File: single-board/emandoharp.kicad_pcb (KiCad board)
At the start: 2 copper layers, 120 x 170 mm, 117 parts, among them P1 piezo, P10 piezo, P11 piezo, P12 piezo, P13 piezo, P14 piezo, P15 piezo, P16 piezo, P17 piezo, P18 piezo, P19 gnd, P2 piezo, P20 gnd, P21 gnd, P22 gnd, P23 gnd, P24 gnd, P25 gnd, P26 gnd, P27 gnd, P28 gnd, P29 gnd, P3 piezo, P30 gnd, P31 gnd, P32 gnd, P33 gnd, P34 gnd, P35 gnd, P36 gnd, P4 piezo, P5 piezo, P6 piezo, P7 piezo, P8 piezo, P9 piezo, U1 Teensy4.1

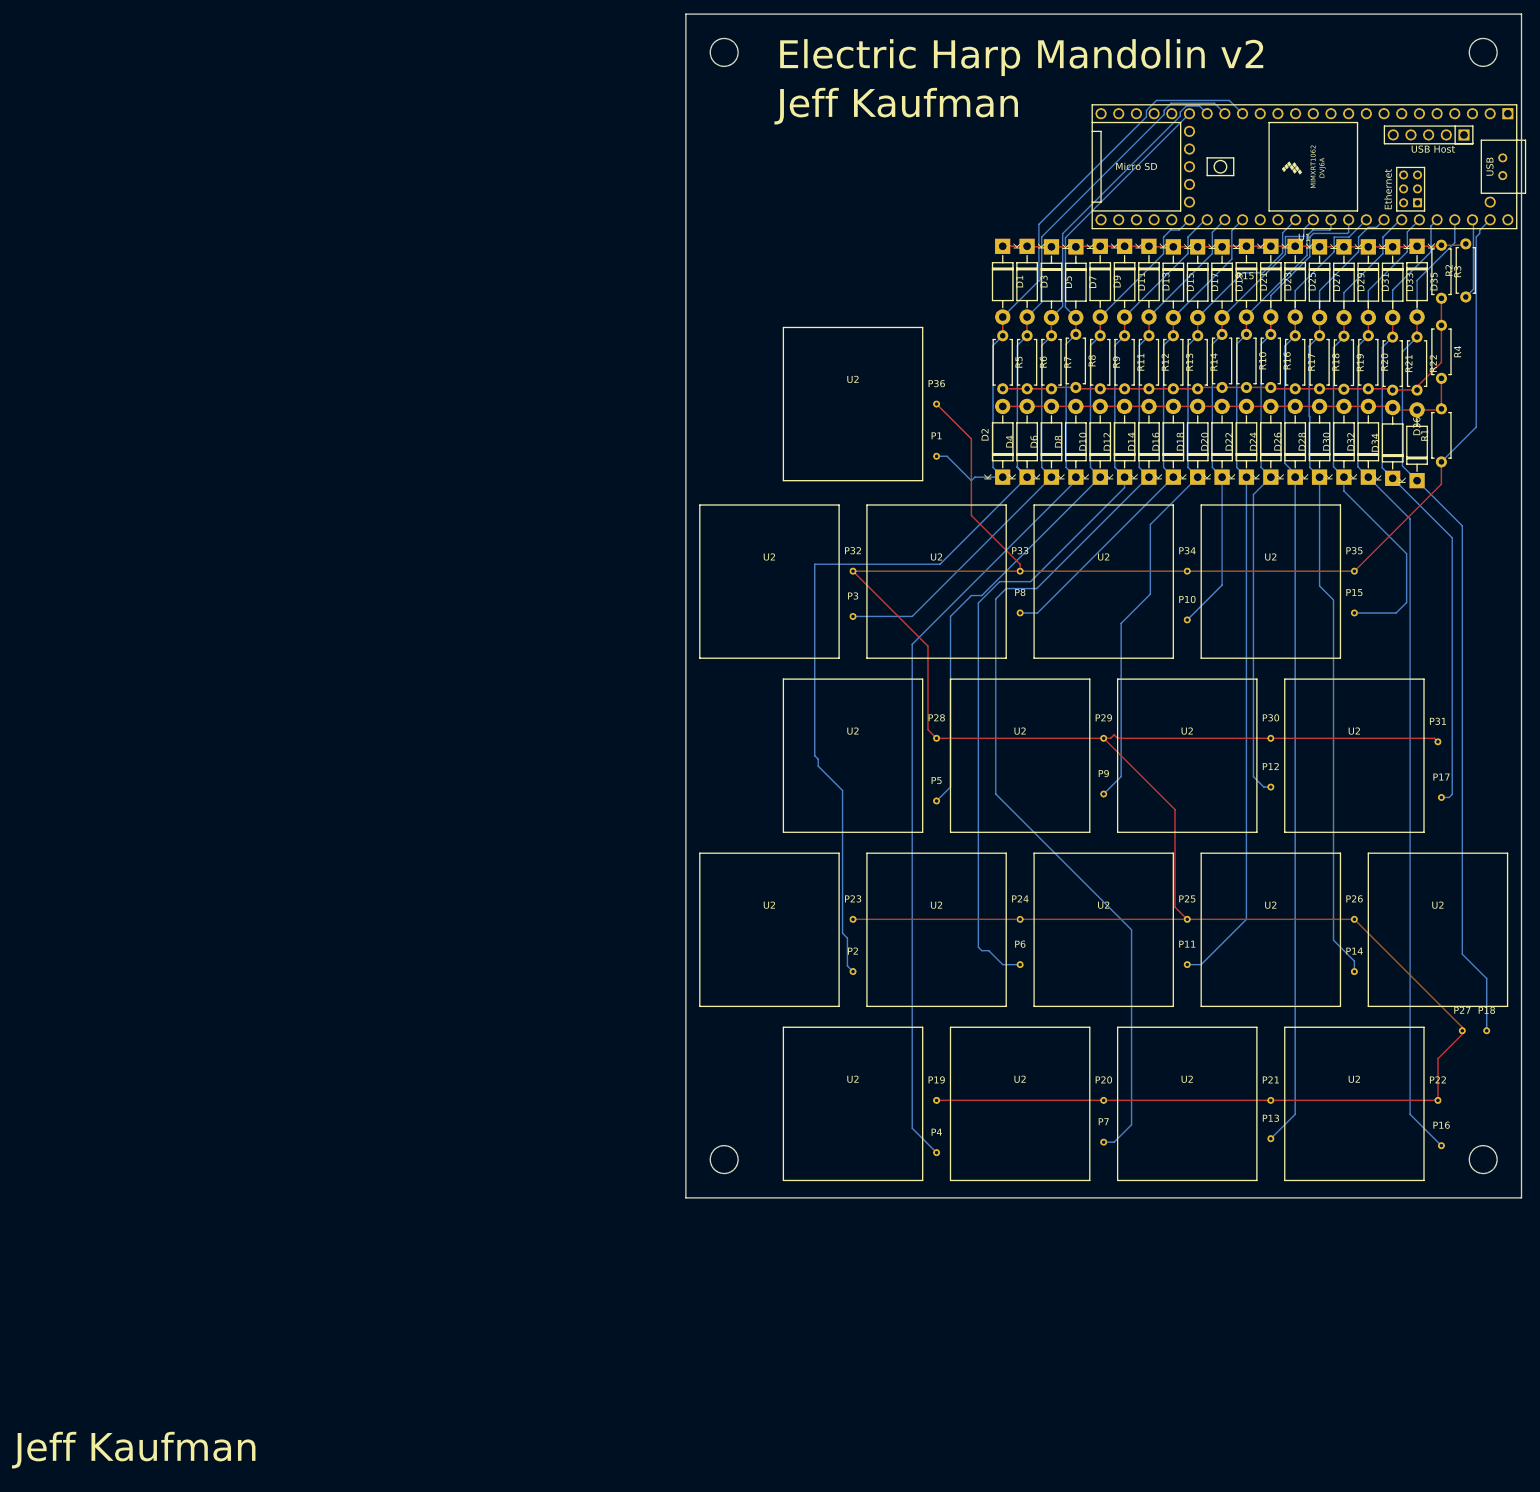
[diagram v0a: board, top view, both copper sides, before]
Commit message: single board: pizeo holes were too small
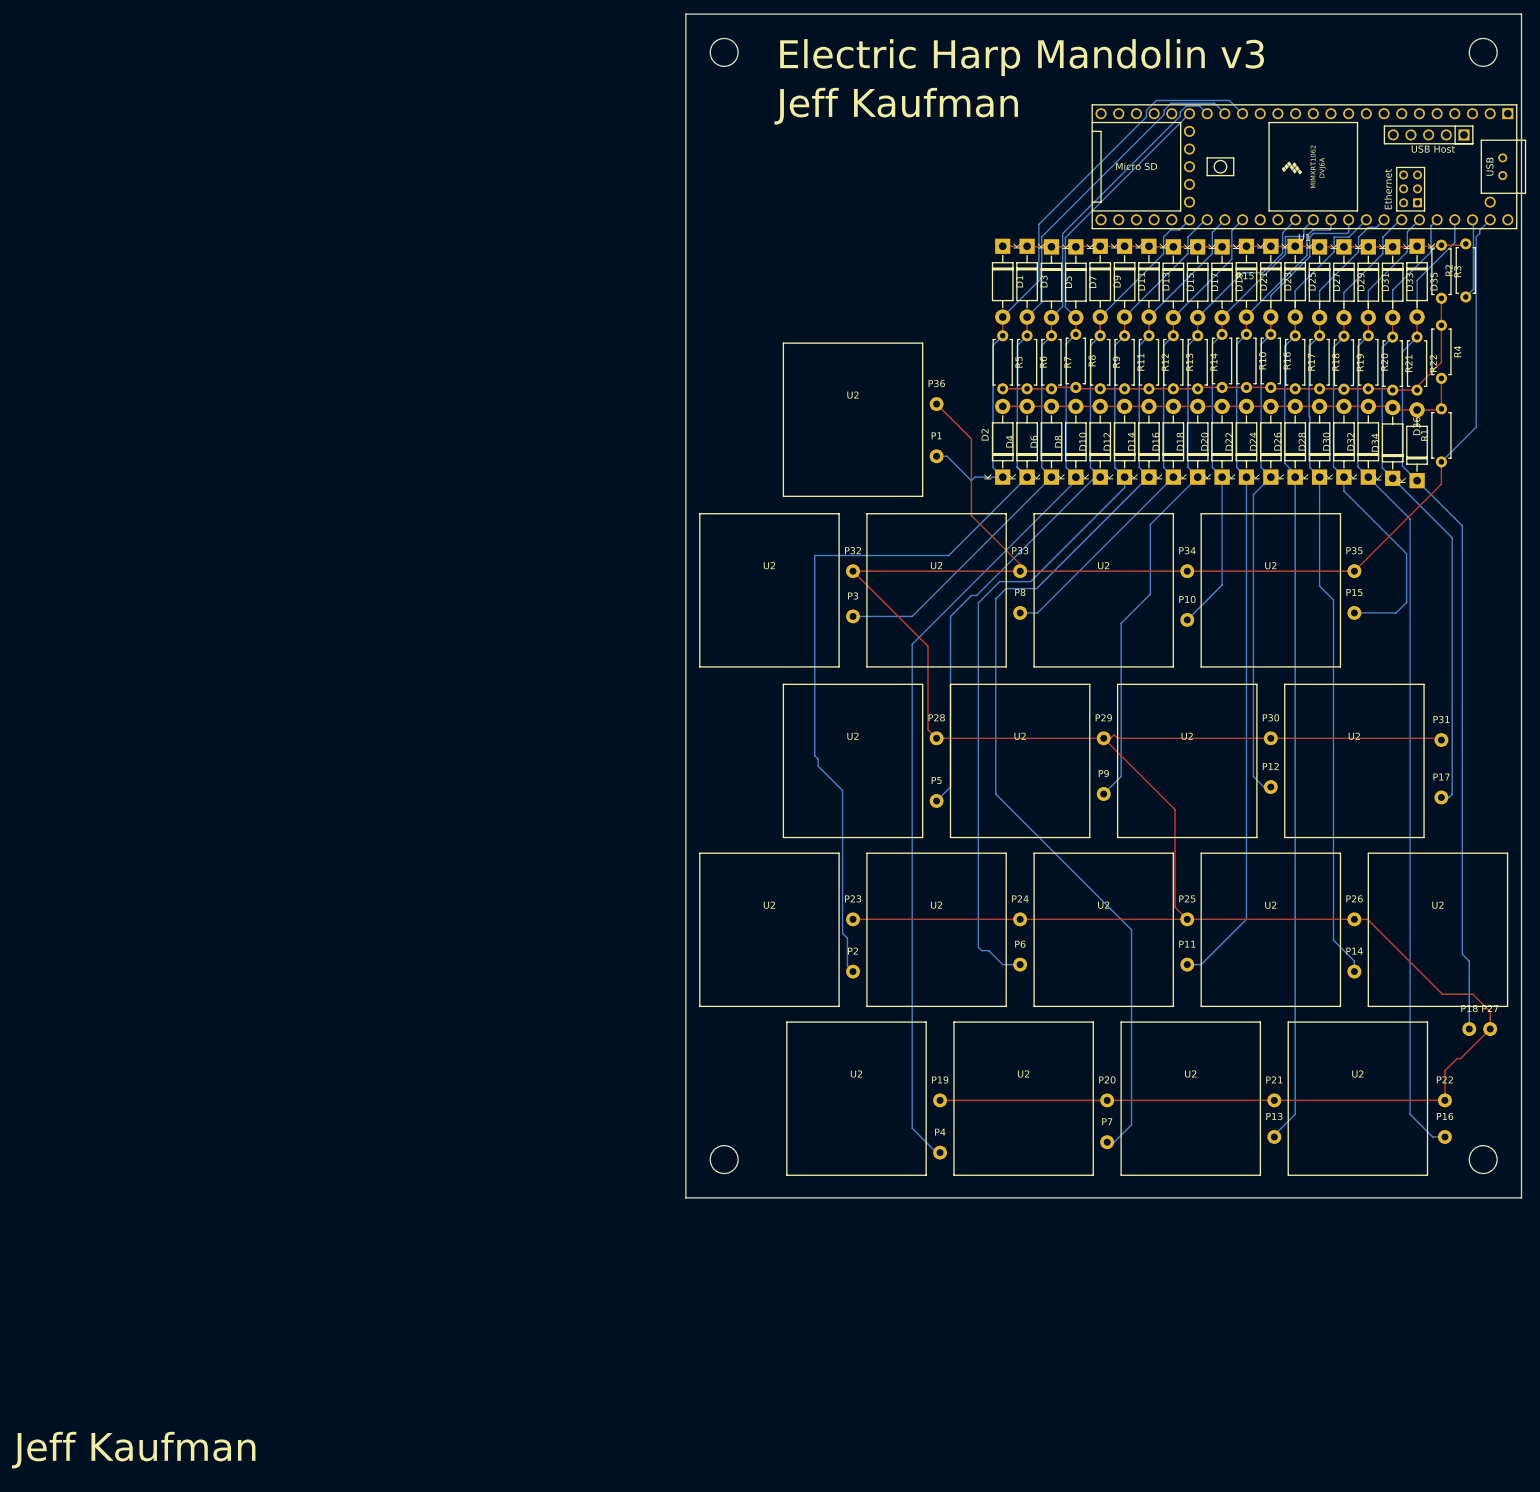
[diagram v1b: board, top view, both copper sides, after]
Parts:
- moved P27 4.01 mm to (141.5, 165.0)
- moved P18 2.51 mm to (138.5, 165.0)
- moved U2 2.25 mm to (50.0, 77.5)
- moved P16 1.35 mm to (135.0, 180.5)
- moved U2 1.25 mm to (110.0, 102.0)
- moved U2 1.25 mm to (38.0, 102.0)
- moved U2 1.25 mm to (86.0, 102.0)
- moved U2 1.25 mm to (62.0, 102.0)
- moved P22 1.00 mm to (135.0, 175.2)
- moved U2 0.90 mm to (50.5, 175.0)
- moved U2 0.90 mm to (74.5, 175.0)
- moved U2 0.90 mm to (98.5, 175.0)
- moved U2 0.90 mm to (122.5, 175.0)
- moved U2 0.75 mm to (74.0, 126.5)
- moved U2 0.75 mm to (122.0, 126.5)
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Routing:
- net Net-(P19-Pad1): track 469.9 -> 477.8 mm
- net Net-(D35-A): track 124.6 -> 123.3 mm
- net Net-(D3-A): track 170.3 -> 171.1 mm
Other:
- board text added: "Electric Harp Mandolin v3"
- board text removed: "Electric Harp Mandolin v2"
